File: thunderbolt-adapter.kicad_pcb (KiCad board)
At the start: 2 copper layers, 70 x 50 mm, 26 parts, among them J1 DX07S024JJ2R1300, J2 PCIe_x4_Conn_EdgeMount, U3 TPS65983BAZBHR, U4 JHL6340SLLSQ, U5 MX25L8006EM1I-12G, U6 SI52112-B6-GT, Y1 ABM8G-25.000MHZ-B4Y-T, Y2 ABM8G-25.000MHZ-B4Y-T

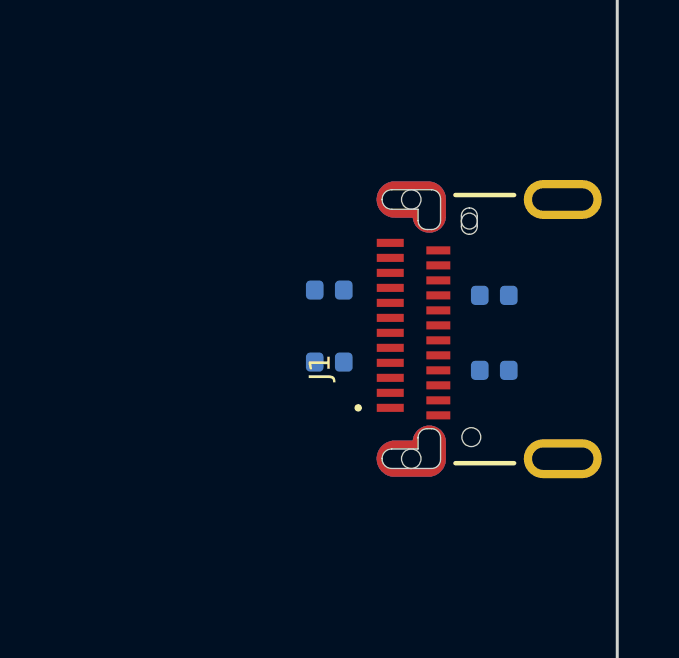
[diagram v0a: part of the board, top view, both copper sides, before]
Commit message: Temporarily removed USB-C connector
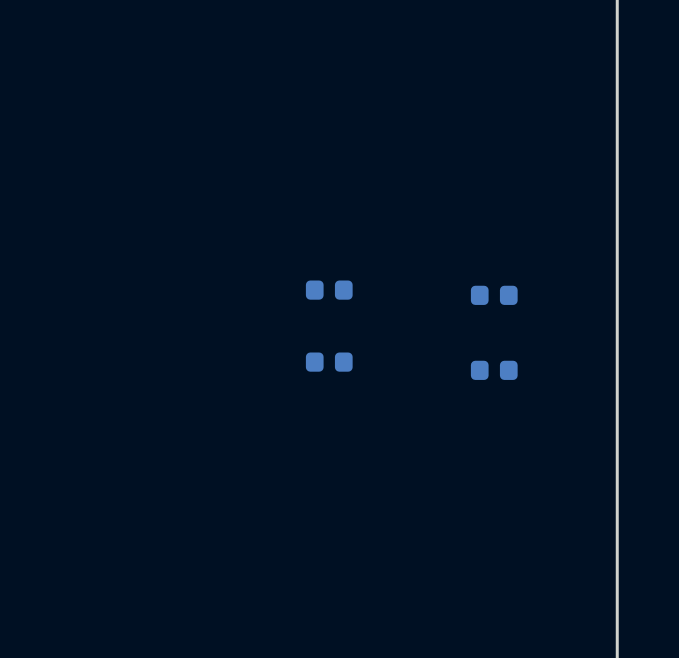
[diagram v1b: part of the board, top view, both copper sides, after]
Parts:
- removed J1: DX07S024JJ2R1300, antmicro-footprints:DX07S024JJ2R1300
